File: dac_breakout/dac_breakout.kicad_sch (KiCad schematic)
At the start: 21 parts, among them J101 Conn_Coaxial_x2, J102 Conn_02x06_Odd_Even, U101 PCM5102A, U102 AZ1117-3.3

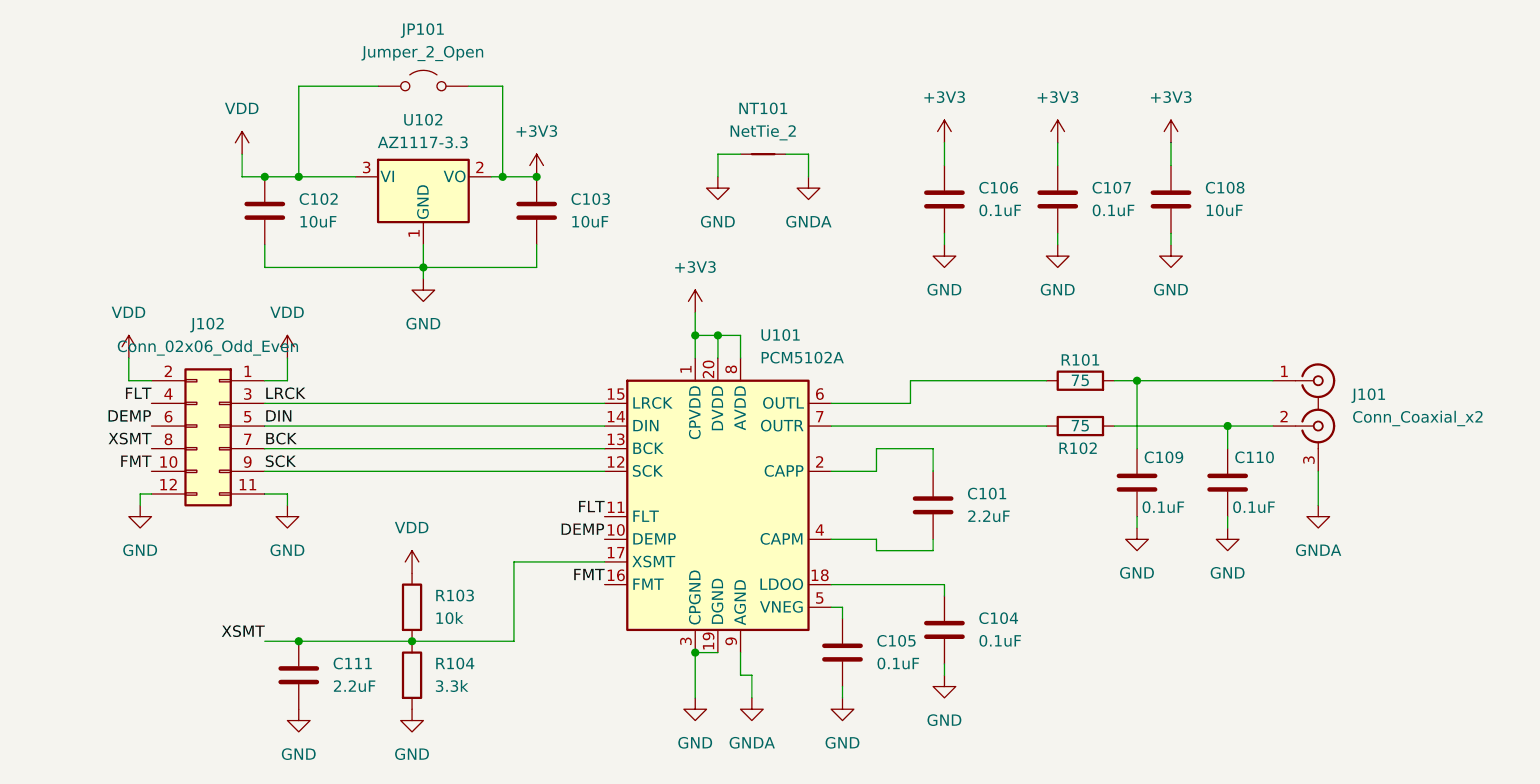
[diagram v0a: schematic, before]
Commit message: Made breakboard compatible
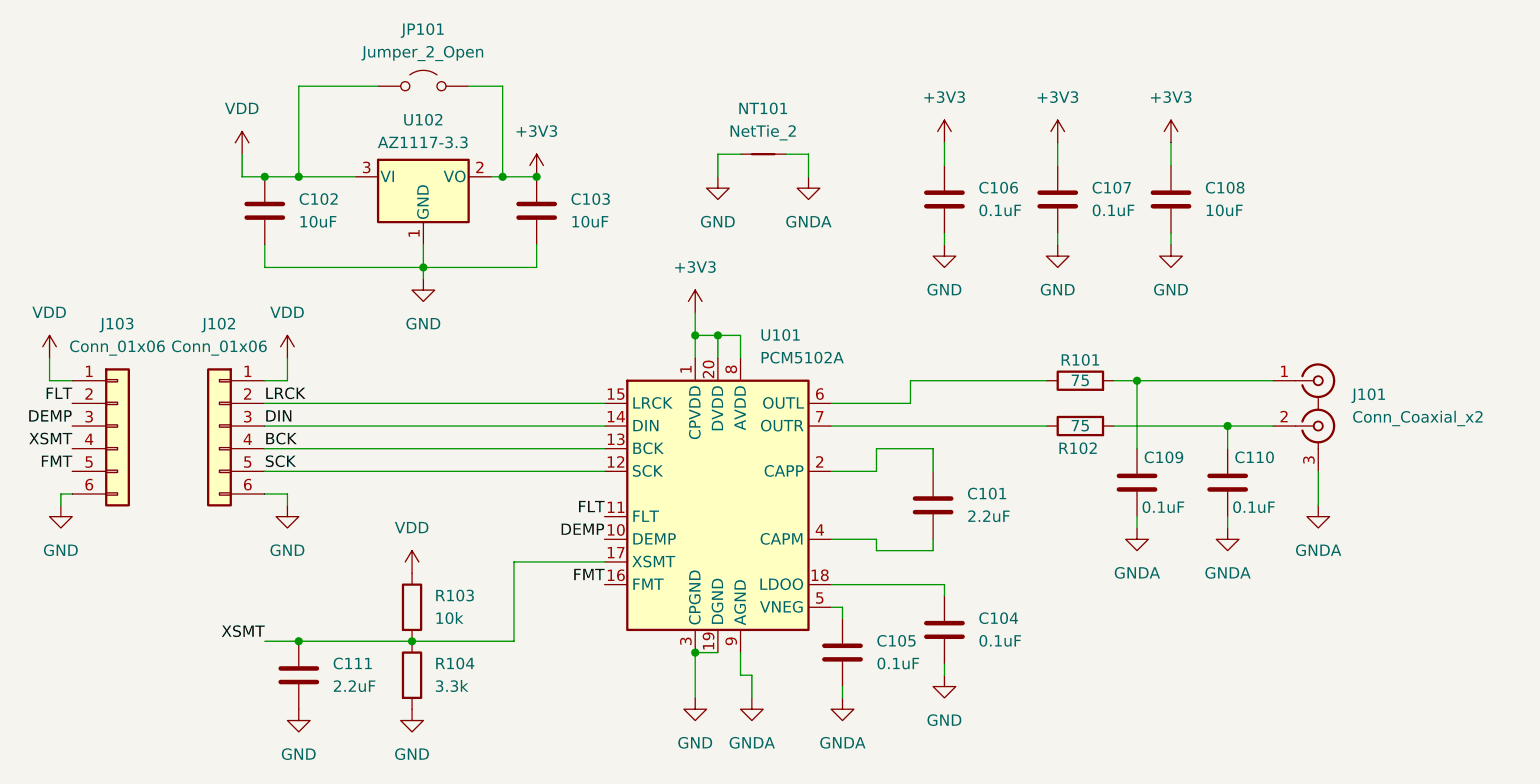
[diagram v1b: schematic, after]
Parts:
- removed J102: Conn_02x06_Odd_Even, Connector_PinHeader_2.54mm:PinHeader_2x06_P2.54mm_Vertical, symbol Connector_Generic:Conn_02x06_Odd_Even
- added J102, J103: Conn_01x06, Connector_PinHeader_2.54mm:PinHeader_1x06_P2.54mm_Vertical, symbol Connector_Generic:Conn_01x06
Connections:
- net BCK: now also J102.4 (Pin_4)
- net DEMP: now also J103.3 (Pin_3)
- net DIN: now also J102.3 (Pin_3)
- net FLT: now also J103.2 (Pin_2)
- net FMT: now also J103.5 (Pin_5)
- net GND: now also J102.6 (Pin_6), J103.6 (Pin_6); no longer C105.2, C109.2, C110.2
- net GNDA: now also C105.2, C109.2, C110.2
- net LRCK: now also J102.2 (Pin_2)
- net SCK: now also J102.5 (Pin_5)
- net VDD: now also J102.1 (Pin_1), J103.1 (Pin_1)
- net XSMT: now also J103.4 (Pin_4)
